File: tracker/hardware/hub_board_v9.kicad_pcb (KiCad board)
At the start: 4 copper layers, 70 x 70 mm, 59 parts, among them Q1 52MHz, U1 ESP32-S3-WROOM-1U-N8R8, U2 LoRa2021F33-2G4, U3 LoRa2021_Castellated, U4 SX1280, U5 MAX-M10S, U6 MS5611-01BA, U7 TPS7A02

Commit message: fix(fab): SX1280 exposed pad renumbered 25 -> 0; U4 GND return now ASSIGNED
OPERATOR-APPROVED one-line footprint change, now verified complete.

THE DEFECT. The footprint numbered the exposed/thermal pad '25'; the symbol numbered the same pad '0'.
KiCad binds pads BY NUMBER, so pad 25 matched no netlist node and sat with an EMPTY net. The netlist
always intended GND:
    GND   U4 pins ['0', '13', '20', '21', '23', '24', '5']
So the SX1280's primary ground and thermal return was unassigned on the board.

THE EDIT, and it is literally one line (footprint diff, 128c128):
    -  (pad "25" smd rect (at 0.00 0.00) (size 2.70 2.70)
    +  (pad "0"  smd rect (at 0.00 0.00) (size 2.70 2.70)
Exactly one occurrence existed, asserted before replacing.

GATE (gate_ep_renumber.py, written BEFORE the edit -- all seven checks PASS):
    1  one empty-net pad before, = '25', 2.70x2.70      PASS
    2  zero empty-net pads after                         PASS
    3  pad '0' now exists at the old '25' position       PASS
    4a '25' no longer exists                             PASS
    4b 24 perimeter pads unchanged (SET equality)        PASS
    5  pad '0' carries GND                               PASS
    6  pad count unchanged (25)                          PASS
Checks 3-6 are set comparisons, not counts: a count would pass if a pad were renamed twice.

A REAL MISTAKE MADE AND CAUGHT, worth recording. Renumbering required REBUILDING U4 from the
corrected library footprint. `pcbnew.FootprintLoad` returns pad NUMBERS and GEOMETRY but NO NETS, so
after re-adding it the perimeter pads all had an empty net -- U4 went from 1 empty-net pad to 24. The
gate caught it (check 2 failed) and the fix was restore_u4_nets.py: take pad nets from the PRE-EDIT
board by pad number, and the EP's net from the netlist. Evaluation ORDER mattered: rebuilding first
and binding nets second is the wrong order, and only the gate revealed it.

ALSO MEASURED, and it corrects an over-broad reading of the gate: this bo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
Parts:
- U4: footprint balloon_flight_v9:SX1280_QFN24 -> SX1280_QFN24
- moved L1 53.6 mm to (55.5, 30.7)
- moved C0 16.9 mm to (52.5, 30.7)

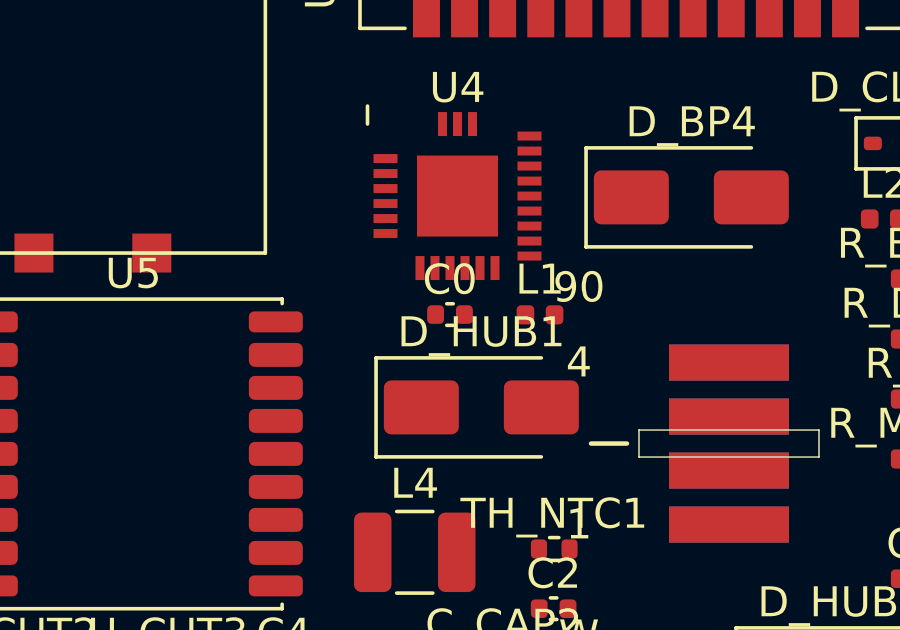
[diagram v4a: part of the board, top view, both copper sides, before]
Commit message: fix(fab): C0 ROTATED 180 deg -- DRC-confirmed removal of the RF short, leg shortened 3.00 -> 2.04 mm
CONFIRMED BY THE GRADER, NOT BY ARITHMETIC. test_c0_rotation.py laid the two RF legs as real tracks and
graded each variant with kicad-cli. Three of my own geometry tools had been wrong on this question, so
this test models nothing -- it moves the part, lays the copper, and asks the DRC.

    variant             errors  delta  shorting_items  clearance  legs (mm)
    control (no tracks)   235     --        0            110        --
    rot0  (as placed)     240     +5        1            113    (1.62, 3.00, 2.96)
    rot180                238     +3        0            113    (1.62, 2.04, 2.96)

APPLIED: C0 orientation 0.0 -> 180.0 deg. Its RF pad moves (52.02, 30.70) -> (52.98, 30.70), i.e. to
the L1 side, which takes C0's GND pad OFF the pad22-to-L1 path.

WHY IT WORKS: C0 is a two-terminal shunt (pad1 = /SX1280_RF, pad2 = GND). As placed, pad2 sat between
U4.pad22 and L1's series pad, so routing the node shorted. Rotating 180 degrees puts the RF terminal on
the path side.

RESULTING NODE GEOMETRY:
    pad22 -> C0.RF   1.62 mm
    C0.RF -> L1.RF   2.04 mm   (was 3.00 mm)

DELIBERATE NON-CLAIM. The rotated board's DRC reports 27 errors (copper_edge_clearance 24,
starved_thermal 3, shorting_items 0). That is NOT an improvement over the 235 figure quoted elsewhere
in this session and must not be presented as one: this board has NO TRACKS REFILLED, whereas the 235
figure came from a board with 110 `clearance` and 89 `solder_mask_bridge` errors arising from ROUTED
COPPER. The two numbers count different things. The valid comparisons are the same-shape ones in the
table above, where control and variants differ ONLY by the RF legs.

NOT DONE: no track is laid on /SX1280_RF. The rotation makes the net ROUTABLE; building the trace is a
separate step. The required width is still unknown because the 0.6 mm stackup is undeclared (the
50-ohm width spans a factor of 3.7 across 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
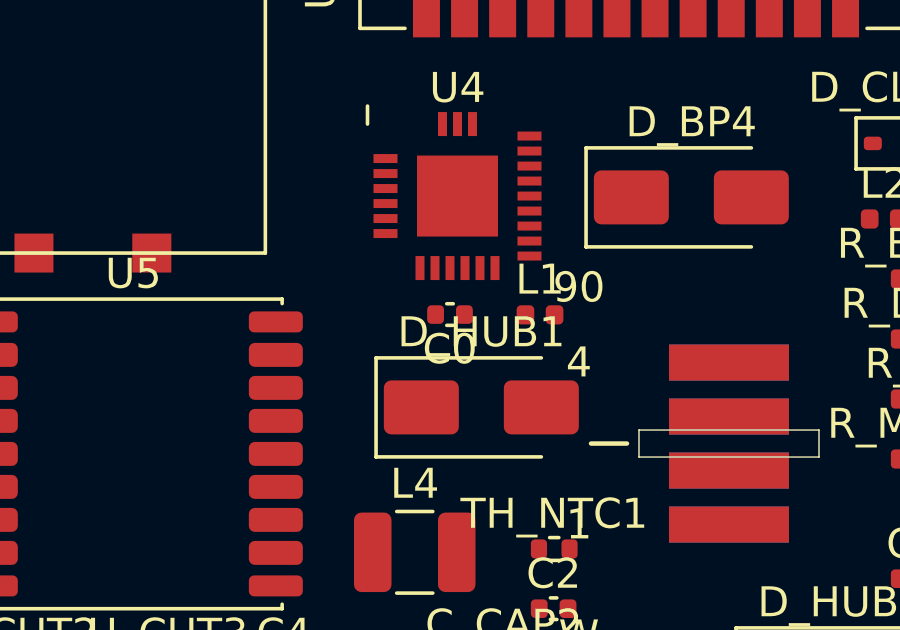
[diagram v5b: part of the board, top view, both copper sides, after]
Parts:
- turned C0 to 180 degrees
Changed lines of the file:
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@@
 	(footprint "Capacitor_SMD:C_0402_1005Metric"
 		(layer "F.Cu")
-		(at 52.5 30.7)
+		(at 52.5 30.7 180)
 		(descr "Capacitor SMD 0402 (1005 Metric), square (rectangular) end terminal, IPC-7351 nominal, (Body size source: IPC-SM-782 page 76, https://www.pcb-3d.com/wordpress/wp-content/uploads/ipc-sm-782a_amendment_1_and_2.pdf), generated with kicad-footprint-generator")
 		(tags "capacitor")
 		(property "Reference" "C0"
-			(at 0 -1.16 0)
+			(at 0 -1.16 180)
 			(layer "F.SilkS")
 			(effects
@@
 		)
 		(property "Value" "0.8pF"
-			(at 0 1.16 0)
+			(at 0 1.16 180)
 			(layer "F.Fab")
 			(effects
@@
 		)
 		(property "Datasheet" ""
-			(at 0 0 0)
+			(at 0 0 180)
 			(layer "F.Fab")
 			(hide yes)
@@
 		)
 		(property "Description" ""
-			(at 0 0 0)
+			(at 0 0 180)
 			(layer "F.Fab")
 			(hide yes)
@@
 		(attr smd)
 		(fp_line
-			(start -0.107836 -0.36)
-			(end 0.107836 -0.36)
+			(start -0.107836 0.36)
+			(end 0.107836 0.36)
 			(stroke
 				(width 0.12)
@@
 		)
 		(fp_line
-			(start -0.107836 0.36)
-			(end 0.107836 0.36)
+			(start -0.107836 -0.36)
+			(end 0.107836 -0.36)
 			(stroke
 				(width 0.12)
@@
 		)
 		(fp_text user "${REFERENCE}"
-			(at 0 0 0)
+			(at 0 0 180)
 			(layer "F.Fab")
 			(effects
@@
 		)
 		(pad "1" smd roundrect
-			(at -0.48 0)
+			(at -0.48 0 180)
 			(size 0.56 0.62)
 			(layers "F.Cu" "F.Mask" "F.Paste")
@@
 		)
 		(pad "2" smd roundrect
-			(at 0.48 0)
+			(at 0.48 0 180)
 			(size 0.56 0.62)
 			(layers "F.Cu" "F.Mask" "F.Paste")

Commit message: fix(fab): /SX1280_RF ROUTED -- C0 nudged 0.4mm left, DRC-clean, board improves to 26 errors
THE RESULT, graded by refilled DRC:
    CONTROL (refilled, no RF tracks):  27  {copper_edge_clearance 24, starved_thermal 3}
    ROUTED  (C0 nudged, 2 legs):       26  {copper_edge_clearance 24, starved_thermal 2}
    delta -1.  clearance 0.  shorting_items 0.  solder_mask_bridge 0.  no new class.

The routed board is one error BETTER than the unrouted control: it adds no fault and drops a
starved_thermal. GATE PASS.

THE FIX: move C0 by (-0.4, 0.0) mm, i.e. 52.50 -> 52.10 in x. Its RF pad lands at (52.58, 30.70),
essentially the same x as U4.pad22 (52.50), so the leg runs nearly STRAIGHT DOWN instead of diagonally
past U4.pad21.

WHY THAT, AND NOT A NARROWER TRACE. The straight leg pad22 -> C0.RF initially measured 0.116 mm from
U4.pad21 against a 0.200 mm floor. Narrowing was tested first and is provably insufficient:

    w1 = 0.200 mm  ->  gap 0.1160 mm
    w1 = 0.100 mm  ->  gap 0.1660 mm      (improves by exactly half the width reduction)
    required           0.2000 mm
Extrapolating, the gap reaches 0.200 mm only at width 0.000 mm. So the PATH was wrong, not the width,
and no trace width can satisfy the floor on that diagonal. Moving C0 swings the path clear.

FOUND BY SWEEP, NOT BY ARITHMETIC. move_c0_for_clearance.py tested 50 offsets of C0, grading EACH with a
refilled DRC. Exactly one point was clean: (-0.4, 0.0). Every neighbouring offset added at least one new
class -- clearance, shorting_items, solder_mask_bridge or courtyards_overlap. So this is not a lucky
pick from a flat landscape; it is the single clean point found in that sweep. Had I reasoned about it
instead, I would have produced another of this session's wrong answers: three of my own geometry tools
were already wrong on this exact question.

PROCESS NOTES THAT MADE THIS WORK, both learned the hard way this session:
  1. REFILL BEFORE EVERY DRC. The board's "235 errors" were 208 stale zone fill; every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
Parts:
- moved C0 0.40 mm to (52.1, 30.7)
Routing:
- net /SX1280_RF: track 0.00 -> 3.99 mm
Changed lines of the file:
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@@
 	(footprint "Capacitor_SMD:C_0402_1005Metric"
 		(layer "F.Cu")
-		(at 52.5 30.7 180)
+		(at 52.1 30.7 180)
 		(descr "Capacitor SMD 0402 (1005 Metric), square (rectangular) end terminal, IPC-7351 nominal, (Body size source: IPC-SM-782 page 76, https://www.pcb-3d.com/wordpress/wp-content/uploads/ipc-sm-782a_amendment_1_and_2.pdf), generated with kicad-footprint-generator")
 		(tags "capacitor")
@@
 		(layer "Edge.Cuts")
 	)
+	(segment
+		(start 52.5 29.15)
+		(end 52.58 30.7)
+		(width 0.2)
+		(layer "F.Cu")
+		(net 40)
+	)
+	(segment
+		(start 52.58 30.7)
+		(end 55.015 30.71)
+		(width 0.2)
+		(layer "F.Cu")
+		(net 40)
+	)
 	(zone
